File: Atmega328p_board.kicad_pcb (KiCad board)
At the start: 2 copper layers, 48.2 x 30.3 mm, 30 parts, among them J1 Conn_01x04_Pin, J2 Conn_01x04_Pin, J3 Conn_01x09_Pin, J4 Conn_02x03_Odd_Even, U1 24LC1025, U2 24LC1025, U3 ATMEGA328P-AU, U4 DS1337S_, Y1 16MHz, Y2 32.768 KHz

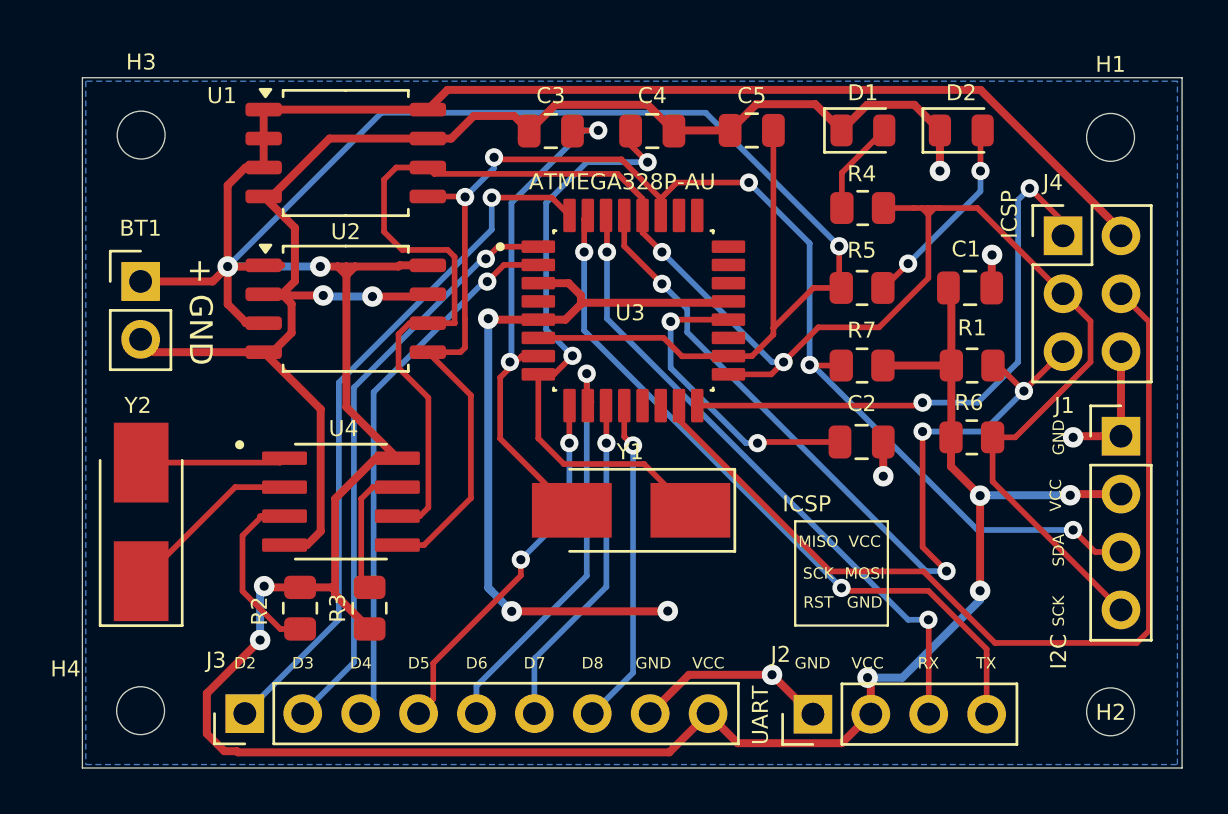
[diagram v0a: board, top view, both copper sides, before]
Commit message: 2 layer pcb fixed with changes of sck and scl
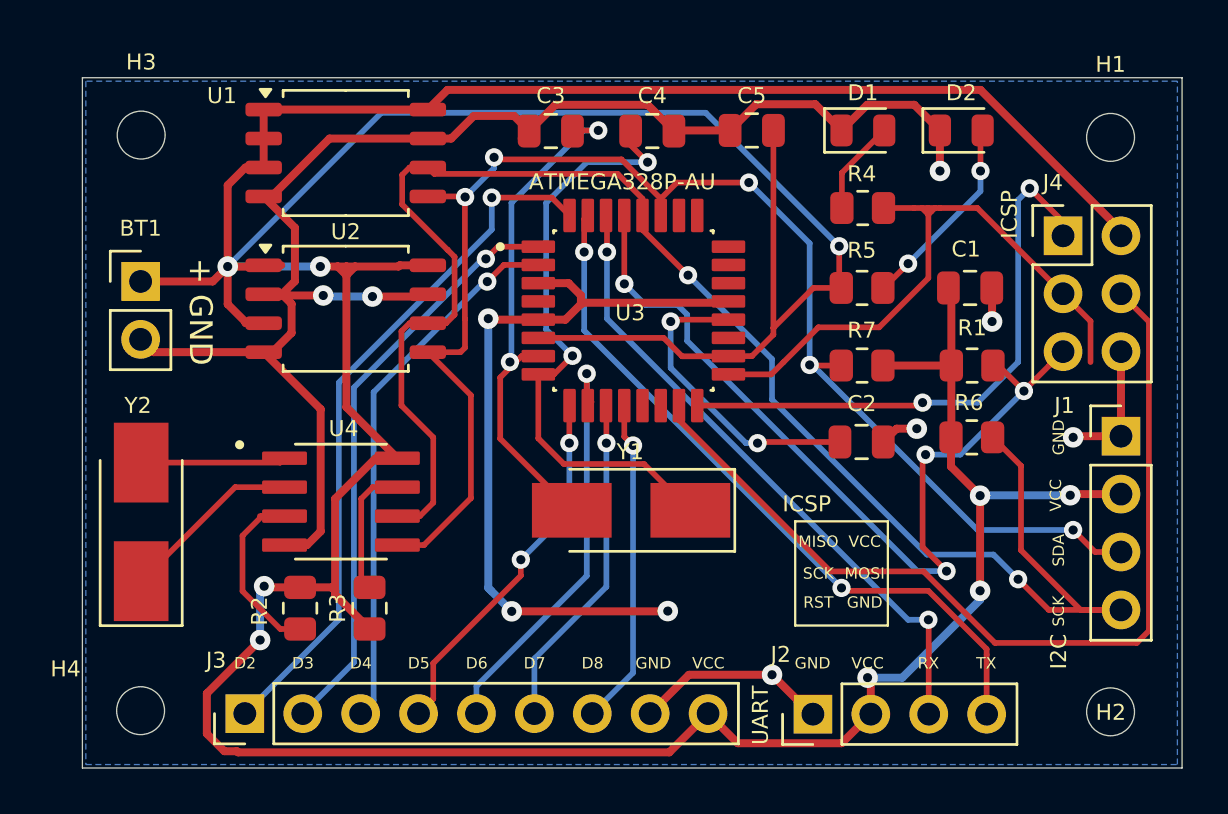
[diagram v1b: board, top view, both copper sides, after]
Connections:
- J1 pad 4: /SCK -> /SCL
- R6 pad 2: /SCK -> /SCL
- U1 pad 6: /SCK -> /SCL
- U2 pad 6: /SCK -> /SCL
- U3 pad 28: /SCK -> /SCL
- U4 pad 6: /SCK -> /SCL
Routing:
- net /SCL: track 0.00 -> 72.1 mm, vias 0 -> 2
- net /SCK: track 86.5 -> 27.7 mm, vias 2 -> 0
